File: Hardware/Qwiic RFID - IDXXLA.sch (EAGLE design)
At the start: 34 parts, among them J2 SMD, J3 PTH, J4 SMD, J8 AVR_SPI_PROG_3X2TESTPOINTS, Q1 600mA/40V, U1 ATTINY84, U2 ID-12/20SMD

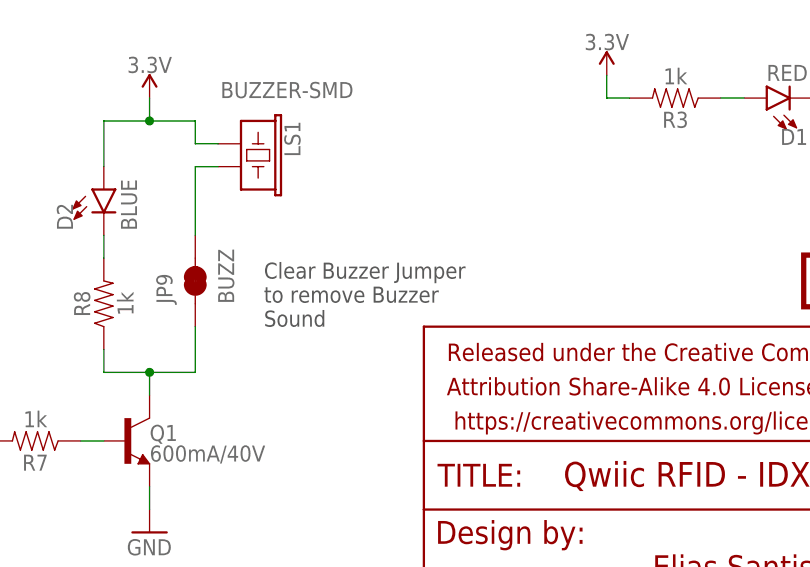
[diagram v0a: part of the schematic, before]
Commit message: More compact
Shrunk 10 mil, beefed up 3.3V lines to 10 mil
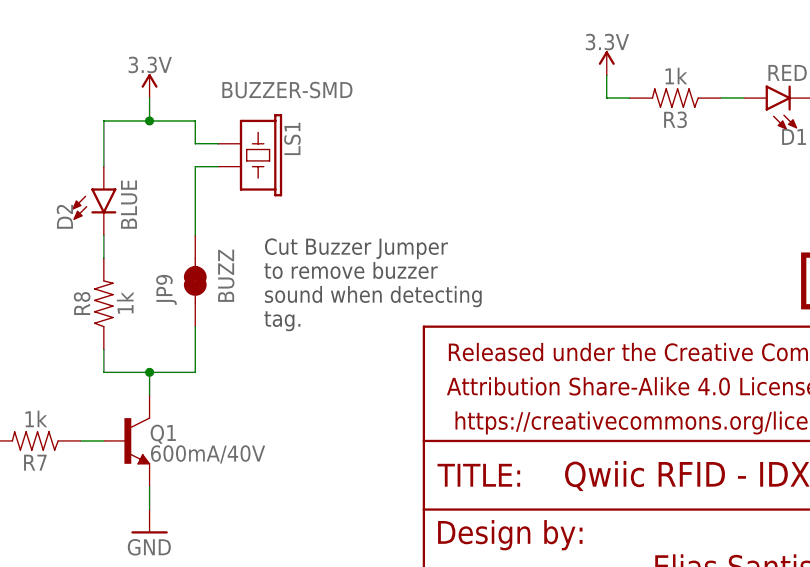
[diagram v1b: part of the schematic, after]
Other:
- note added: "Cut Buzzer Jumper to remove buzzer sound when detecting tag."
- note removed: "Clear Buzzer Jumper to remove Buzzer Sound"
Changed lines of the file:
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@@
 Closed Jumper: 0x7C
 Software configurable as well</text>
-<text x="129.54" y="35.56" size="1.778" layer="97">Clear Buzzer Jumper
-to remove Buzzer
-Sound</text>
+<text x="129.54" y="35.56" size="1.778" layer="97">Cut Buzzer Jumper
+to remove buzzer
+sound when detecting
+tag.</text>
 <text x="116.84" y="111.76" size="1.778" layer="97" font="vector">Cut INT jumper
 to remove

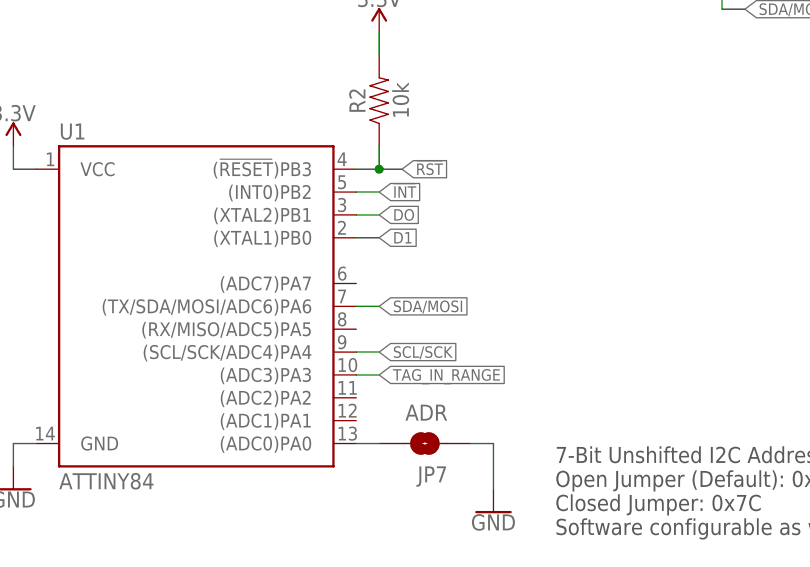
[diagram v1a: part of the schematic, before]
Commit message: 5 mil smaller
Moved power LED around, squished the PCB a little more.
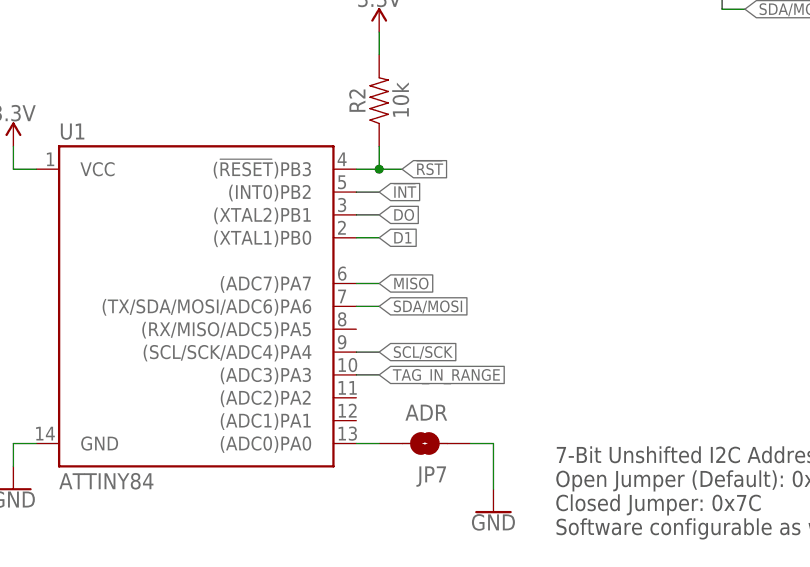
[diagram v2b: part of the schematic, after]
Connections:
- net MISO: now also U1.(ADC7)PA7
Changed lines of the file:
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@@
 <label x="43.18" y="175.26" size="1.27" layer="95" font="vector" rot="R180" xref="yes"/>
+</segment>
+<segment>
+<pinref part="U1" gate="U1" pin="(ADC7)PA7"/>
+<wire x1="60.96" y1="119.38" x2="63.5" y2="119.38" width="0.1524" layer="91"/>
+<label x="63.5" y="119.38" size="1.27" layer="95" xref="yes"/>
 </segment>
 </net>

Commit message: Moved RST clost to INT PTH, better routing
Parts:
- added C1: 0.1uF, SparkFun-Capacitors:0.1UF-0603-25V-(+80/-20%)
- U1: value ATTINY84 -> ATTINY84-ARDUINO; device SparkFun-IC-Microcontroller:ATTINY84 -> SparkFun-IC-Microcontroller:ATTINY84-ARDUINO
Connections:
- removed net D1: U1.(XTAL1)PB0, U2.D1
- removed net DO: U1.(XTAL2)PB1, U2.D0
- new net DATA_UART: U1.(XTAL2)9, U2.D0
- net !INT: now also U1.(A3)3; no longer U1.(INT0)PB2
- net !RST: now also U1.(!RESET!)11; no longer U1.(!RESET!)PB3
- net 3.3V: now also C1.1
- net GND: now also C1.2
- net MISO: now also U1.(TX/MISO/A5)~5; no longer U1.(ADC7)PA7
- net N$6: now also U1.(A0)0; no longer U1.(ADC0)PA0
- net SCL/SCK: now also U1.(SCL/SCK/A4)4; no longer U1.(SCL/SCK/ADC4)PA4
- net SDA/MOSI: now also U1.(RX/SDA/MOSI/A6)~6; no longer U1.(TX/SDA/MOSI/ADC6)PA6
- net TAG_IN_RANGE: now also U1.(INT0)~8; no longer U1.(ADC3)PA3
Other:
- note added: "Do not use ANT1 or ANT2 unless using ID-2LA"
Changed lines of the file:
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@@
 <part name="GND5" library="SparkFun-PowerSymbols" deviceset="GND" device=""/>
 <part name="JP8" library="SparkFun-Jumpers" deviceset="JUMPER-SMT_2_NC_TRACE" device="_SILK" value="INT"/>
-<part name="U1" library="SparkFun-IC-Microcontroller" deviceset="ATTINY84" device="" value="ATTINY84"/>
+<part name="U1" library="SparkFun-IC-Microcontroller" deviceset="ATTINY84-ARDUINO" device="" value="ATTINY84-ARDUINO"/>
 <part name="GND1" library="SparkFun-PowerSymbols" deviceset="GND" device=""/>
 <part name="SUPPLY5" library="SparkFun-PowerSymbols" deviceset="3.3V" device=""/>
@@
 <part name="U$4" library="SparkX" deviceset="SPARKX-LOGO" device="3"/>
 <part name="J7" library="SparkFun-Connectors" deviceset="CONN_01" device="PTH_NO_SILK_YES_STOP"/>
+<part name="C1" library="SparkFun-Capacitors" deviceset="0.1UF" device="-0603-25V-(+80/-20%)" value="0.1uF"/>
+<part name="SUPPLY13" library="SparkFun-PowerSymbols" deviceset="3.3V" device=""/>
+<part name="GND11" library="SparkFun-PowerSymbols" deviceset="GND" device=""/>
 </parts>
 <sheets>
@@
 to remove pullup
 resistors.</text>
+<text x="152.4" y="142.24" size="1.778" layer="97" font="vector">Do not use ANT1
+or ANT2 unless
+using ID-2LA</text>
 </plain>
 <instances>
@@
 <instance part="U$4" gate="G$1" x="200.66" y="40.64"/>
 <instance part="J7" gate="G$1" x="68.58" y="22.86" rot="R180"/>
+<instance part="C1" gate="G$1" x="15.24" y="116.84"/>
+<instance part="SUPPLY13" gate="G$1" x="15.24" y="124.46"/>
+<instance part="GND11" gate="1" x="15.24" y="109.22"/>
 </instances>
 <busses>
@@
 <pinref part="SUPPLY12" gate="G$1" pin="3.3V"/>
 </segment>
+<segment>
+<pinref part="C1" gate="G$1" pin="1"/>
+<pinref part="SUPPLY13" gate="G$1" pin="3.3V"/>
+<wire x1="15.24" y1="124.46" x2="15.24" y2="121.92" width="0.1524" layer="91"/>
+</segment>
 </net>
 <net name="GND" class="0">
@@
 <wire x1="116.84" y1="15.24" x2="116.84" y2="17.78" width="0.1524" layer="91"/>
 </segment>
+<segment>
+<pinref part="C1" gate="G$1" pin="2"/>
+<pinref part="GND11" gate="1" pin="GND"/>
+<wire x1="15.24" y1="111.76" x2="15.24" y2="114.3" width="0.1524" layer="91"/>
+</segment>
 </net>
 <net name="SCL" class="0">
@@
 </segment>
 <segment>
-<pinref part="U1" gate="U1" pin="(INT0)PB2"/>
-<wire x1="60.96" y1="129.54" x2="63.5" y2="129.54" width="0.1524" layer="91"/>
-<label x="63.5" y="129.54" size="1.27" layer="95" xref="yes"/>
-</segment>
-<segment>
 <pinref part="JP8" gate="G$1" pin="1"/>
 <wire x1="121.92" y1="124.46" x2="119.38" y2="124.46" width="0.1524" layer="91"/>
 <label x="119.38" y="124.46" size="1.27" layer="95" rot="R180" xref="yes"/>
+</segment>
+<segment>
+<pinref part="U1" gate="U1" pin="(A3)3"/>
+<wire x1="60.96" y1="109.22" x2="63.5" y2="109.22" width="0.1524" layer="91"/>
+<label x="63.5" y="109.22" size="1.27" layer="95" font="vector" xref="yes"/>
 </segment>
 </net>
@@
 <net name="N$6" class="0">
 <segment>
-<pinref part="U1" gate="U1" pin="(ADC0)PA0"/>
+<pinref part="U1" gate="U1" pin="(A0)0"/>
 <pinref part="JP7" gate="G$1" pin="2"/>
 <wire x1="60.96" y1="101.6" x2="63.5" y2="101.6" width="0.1524" layer="91"/>
@@
 </segment>
 <segment>
-<pinref part="U1" gate="U1" pin="(ADC7)PA7"/>
-<wire x1="60.96" y1="119.38" x2="63.5" y2="119.38" width="0.1524" layer="91"/>
-<label x="63.5" y="119.38" size="1.27" layer="95" xref="yes"/>
+<pinref part="U1" gate="U1" pin="(TX/MISO/A5)~5"/>
+<wire x1="60.96" y1="114.3" x2="63.5" y2="114.3" width="0.1524" layer="91"/>
+<label x="63.5" y="114.3" size="1.27" layer="95" font="vector" xref="yes"/>
 </segment>
 </net>
@@
 </segment>
 <segment>
-<pinref part="U1" gate="U1" pin="(SCL/SCK/ADC4)PA4"/>
+<pinref part="U1" gate="U1" pin="(SCL/SCK/A4)4"/>
 <wire x1="60.96" y1="111.76" x2="63.5" y2="111.76" width="0.1524" layer="91"/>
 <label x="63.5" y="111.76" size="1.27" layer="95" font="vector" xref="yes"/>
@@
 </segment>
 <segment>
-<pinref part="U1" gate="U1" pin="(TX/SDA/MOSI/ADC6)PA6"/>
+<pinref part="U1" gate="U1" pin="(RX/SDA/MOSI/A6)~6"/>
 <wire x1="60.96" y1="116.84" x2="63.5" y2="116.84" width="0.1524" layer="91"/>
 <label x="63.5" y="116.84" size="1.27" layer="95" font="vector" xref="yes"/>
@@
 <net name="!RST" class="0">
 <segment>
-<pinref part="U1" gate="U1" pin="(!RESET!)PB3"/>
+<pinref part="U1" gate="U1" pin="(!RESET!)11"/>
 <wire x1="66.04" y1="132.08" x2="63.5" y2="132.08" width="0.1524" layer="91"/>
 <label x="66.04" y="132.08" size="1.27" layer="95" font="vector" xref="yes"/>
@@
 </segment>
 </net>
-<net name="DO" class="0">
-<segment>
-<pinref part="U1" gate="U1" pin="(XTAL2)PB1"/>
+<net name="DATA_UART" class="0">
+<segment>
+<pinref part="U1" gate="U1" pin="(XTAL2)9"/>
 <wire x1="60.96" y1="127" x2="63.5" y2="127" width="0.1524" layer="91"/>
 <label x="63.5" y="127" size="1.27" layer="95" font="vector" xref="yes"/>
@@
 </segment>
 </net>
-<net name="D1" class="0">
-<segment>
-<pinref part="U2" gate="G$1" pin="D1"/>
-<wire x1="215.9" y1="132.08" x2="218.44" y2="132.08" width="0.1524" layer="91"/>
-<label x="218.44" y="132.08" size="1.27" layer="95" font="vector" xref="yes"/>
-</segment>
-<segment>
-<pinref part="U1" gate="U1" pin="(XTAL1)PB0"/>
-<wire x1="60.96" y1="124.46" x2="63.5" y2="124.46" width="0.1524" layer="91"/>
-<label x="63.5" y="124.46" size="1.27" layer="95" font="vector" xref="yes"/>
-</segment>
-</net>
 <net name="TAG_IN_RANGE" class="0">
 <segment>
@@
 </segment>
 <segment>
-<pinref part="U1" gate="U1" pin="(ADC3)PA3"/>
-<wire x1="60.96" y1="109.22" x2="63.5" y2="109.22" width="0.1524" layer="91"/>
-<label x="63.5" y="109.22" size="1.27" layer="95" font="vector" xref="yes"/>
-</segment>
-</net>
+<pinref part="U1" gate="U1" pin="(INT0)~8"/>
+<wire x1="60.96" y1="124.46" x2="63.5" y2="124.46" width="0.1524" layer="91"/>
+<label x="63.5" y="124.46" size="1.27" layer="95" font="vector" xref="yes"/>
+</segment>
+</net>

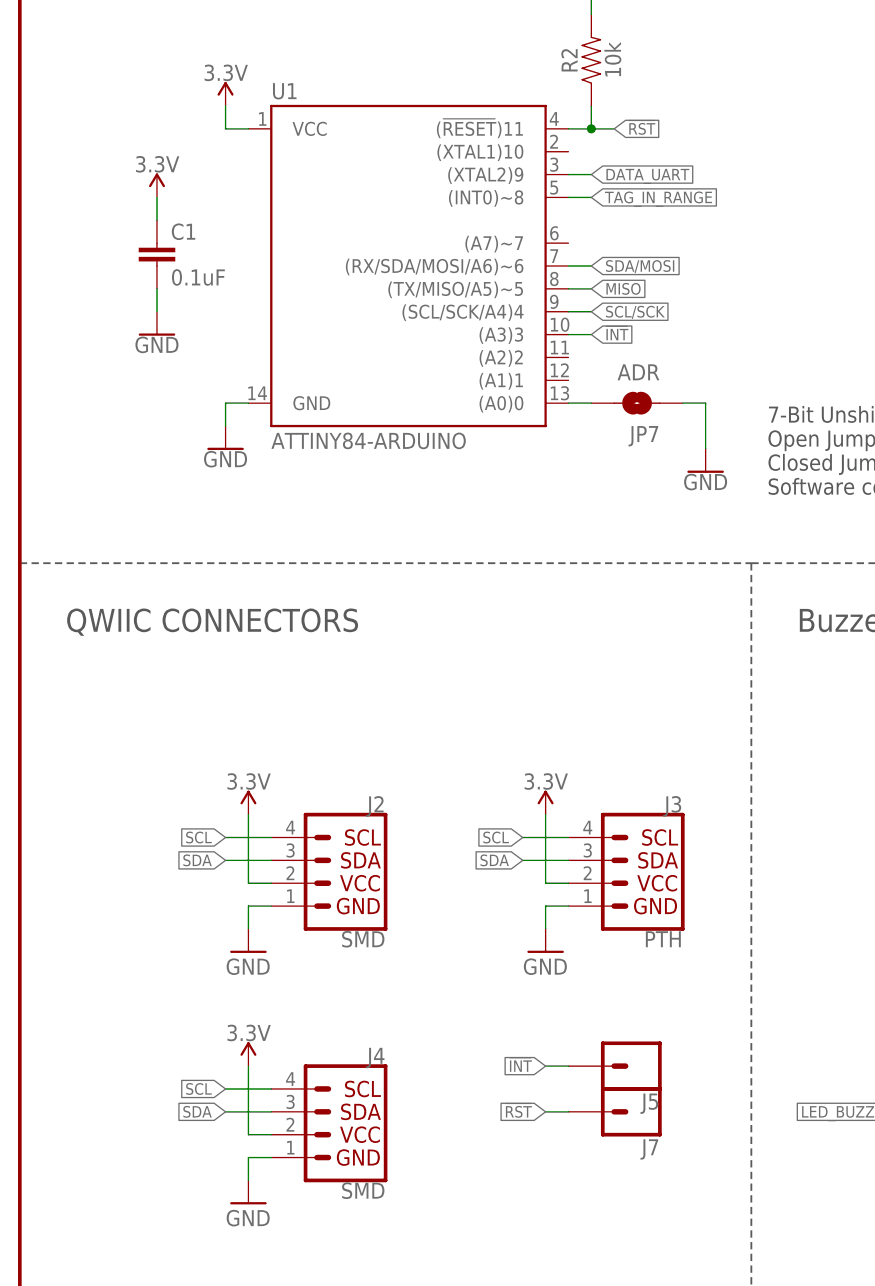
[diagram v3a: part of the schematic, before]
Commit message: Firmware almost finalized, I2C data lines and UART lines fixed on board
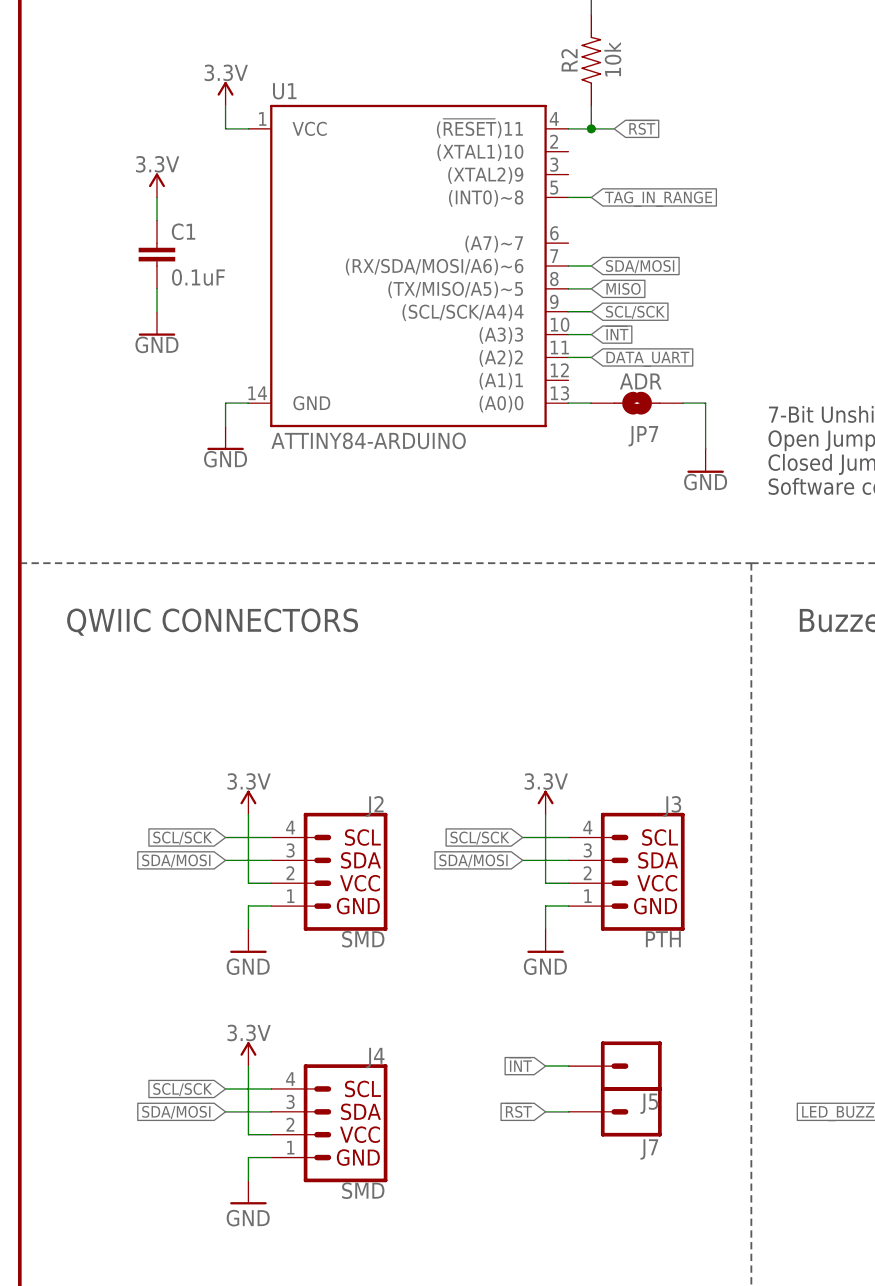
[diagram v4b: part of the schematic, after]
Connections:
- removed net SCL: J2.SCL, J3.SCL, J4.SCL
- removed net SDA: J2.SDA, J3.SDA, J4.SDA
- net DATA_UART: now also U1.(A2)2; no longer U1.(XTAL2)9
- net SCL/SCK: now also J2.SCL, J3.SCL, J4.SCL
- net SDA/MOSI: now also J2.SDA, J3.SDA, J4.SDA
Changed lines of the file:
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@@
 <?xml version="1.0" encoding="utf-8"?>
 <!DOCTYPE eagle SYSTEM "eagle.dtd">
-<eagle version="9.0.1">
+<eagle version="9.1.0">
 <drawing>
 <settings>
@@
 <instance part="SUPPLY10" gate="G$1" x="167.64" y="63.5"/>
 <instance part="D1" gate="G$1" x="185.42" y="60.96" rot="R90"/>
-<instance part="JP7" gate="G$1" x="68.58" y="101.6" rot="R180"/>
+<instance part="JP7" gate="G$1" x="68.58" y="101.6" smashed="yes" rot="R180">
+<attribute name="NAME" x="71.12" y="99.06" size="1.778" layer="95" font="vector" rot="R180"/>
+<attribute name="VALUE" x="71.374" y="103.124" size="1.778" layer="96" font="vector" rot="R180" align="top-left"/>
+</instance>
 <instance part="GND5" gate="1" x="76.2" y="93.98"/>
 <instance part="JP8" gate="G$1" x="127" y="124.46"/>
@@
 </segment>
 </net>
-<net name="SCL" class="0">
-<segment>
-<pinref part="J2" gate="G$1" pin="SCL"/>
-<wire x1="27.94" y1="53.34" x2="22.86" y2="53.34" width="0.1524" layer="91"/>
-<label x="22.86" y="53.34" size="1.27" layer="95" font="vector" rot="R180" xref="yes"/>
-</segment>
-<segment>
-<pinref part="J3" gate="G$1" pin="SCL"/>
-<wire x1="60.96" y1="53.34" x2="55.88" y2="53.34" width="0.1524" layer="91"/>
-<label x="55.88" y="53.34" size="1.27" layer="95" font="vector" rot="R180" xref="yes"/>
-</segment>
-<segment>
-<pinref part="J4" gate="G$1" pin="SCL"/>
-<wire x1="27.94" y1="25.4" x2="22.86" y2="25.4" width="0.1524" layer="91"/>
-<label x="22.86" y="25.4" size="1.27" layer="95" font="vector" rot="R180" xref="yes"/>
-</segment>
-</net>
-<net name="SDA" class="0">
-<segment>
-<pinref part="J2" gate="G$1" pin="SDA"/>
-<wire x1="27.94" y1="50.8" x2="22.86" y2="50.8" width="0.1524" layer="91"/>
-<label x="22.86" y="50.8" size="1.27" layer="95" font="vector" rot="R180" xref="yes"/>
-</segment>
-<segment>
-<pinref part="J3" gate="G$1" pin="SDA"/>
-<wire x1="60.96" y1="50.8" x2="55.88" y2="50.8" width="0.1524" layer="91"/>
-<label x="55.88" y="50.8" size="1.27" layer="95" font="vector" rot="R180" xref="yes"/>
-</segment>
-<segment>
-<pinref part="J4" gate="G$1" pin="SDA"/>
-<wire x1="27.94" y1="22.86" x2="22.86" y2="22.86" width="0.1524" layer="91"/>
-<label x="22.86" y="22.86" size="1.27" layer="95" font="vector" rot="R180" xref="yes"/>
-</segment>
-</net>
 <net name="!INT" class="0">
 <segment>
@@
 <label x="63.5" y="111.76" size="1.27" layer="95" font="vector" xref="yes"/>
 </segment>
+<segment>
+<pinref part="J2" gate="G$1" pin="SCL"/>
+<wire x1="27.94" y1="53.34" x2="22.86" y2="53.34" width="0.1524" layer="91"/>
+<label x="22.86" y="53.34" size="1.27" layer="95" font="vector" rot="R180" xref="yes"/>
+</segment>
+<segment>
+<pinref part="J3" gate="G$1" pin="SCL"/>
+<wire x1="60.96" y1="53.34" x2="55.88" y2="53.34" width="0.1524" layer="91"/>
+<label x="55.88" y="53.34" size="1.27" layer="95" font="vector" rot="R180" xref="yes"/>
+</segment>
+<segment>
+<pinref part="J4" gate="G$1" pin="SCL"/>
+<wire x1="27.94" y1="25.4" x2="22.86" y2="25.4" width="0.1524" layer="91"/>
+<label x="22.86" y="25.4" size="1.27" layer="95" font="vector" rot="R180" xref="yes"/>
+</segment>
 </net>
 <net name="SDA/MOSI" class="0">
@@
 <wire x1="60.96" y1="116.84" x2="63.5" y2="116.84" width="0.1524" layer="91"/>
 <label x="63.5" y="116.84" size="1.27" layer="95" font="vector" xref="yes"/>
+</segment>
+<segment>
+<pinref part="J2" gate="G$1" pin="SDA"/>
+<wire x1="27.94" y1="50.8" x2="22.86" y2="50.8" width="0.1524" layer="91"/>
+<label x="22.86" y="50.8" size="1.27" layer="95" font="vector" rot="R180" xref="yes"/>
+</segment>
+<segment>
+<pinref part="J3" gate="G$1" pin="SDA"/>
+<wire x1="60.96" y1="50.8" x2="55.88" y2="50.8" width="0.1524" layer="91"/>
+<label x="55.88" y="50.8" size="1.27" layer="95" font="vector" rot="R180" xref="yes"/>
+</segment>
+<segment>
+<pinref part="J4" gate="G$1" pin="SDA"/>
+<wire x1="27.94" y1="22.86" x2="22.86" y2="22.86" width="0.1524" layer="91"/>
+<label x="22.86" y="22.86" size="1.27" layer="95" font="vector" rot="R180" xref="yes"/>
 </segment>
 </net>
@@
 <net name="DATA_UART" class="0">
 <segment>
-<pinref part="U1" gate="U1" pin="(XTAL2)9"/>
-<wire x1="60.96" y1="127" x2="63.5" y2="127" width="0.1524" layer="91"/>
-<label x="63.5" y="127" size="1.27" layer="95" font="vector" xref="yes"/>
-</segment>
-<segment>
 <pinref part="U2" gate="G$1" pin="D0"/>
 <wire x1="215.9" y1="134.62" x2="218.44" y2="134.62" width="0.1524" layer="91"/>
 <label x="218.44" y="134.62" size="1.27" layer="95" font="vector" xref="yes"/>
 </segment>
-</net>
+<segment>
+<pinref part="U1" gate="U1" pin="(A2)2"/>
+<wire x1="60.96" y1="106.68" x2="63.5" y2="106.68" width="0.1524" layer="91"/>
+<label x="63.5" y="106.68" size="1.27" layer="95" font="vector" xref="yes"/>
+</segment>
+</net>
